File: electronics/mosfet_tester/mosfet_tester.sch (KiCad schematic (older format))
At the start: 8 parts, among them J101 BARREL_JACK, J102 CONN_01X06, J103 Screw_Terminal_1x01, J104 Screw_Terminal_1x01, U101 7805

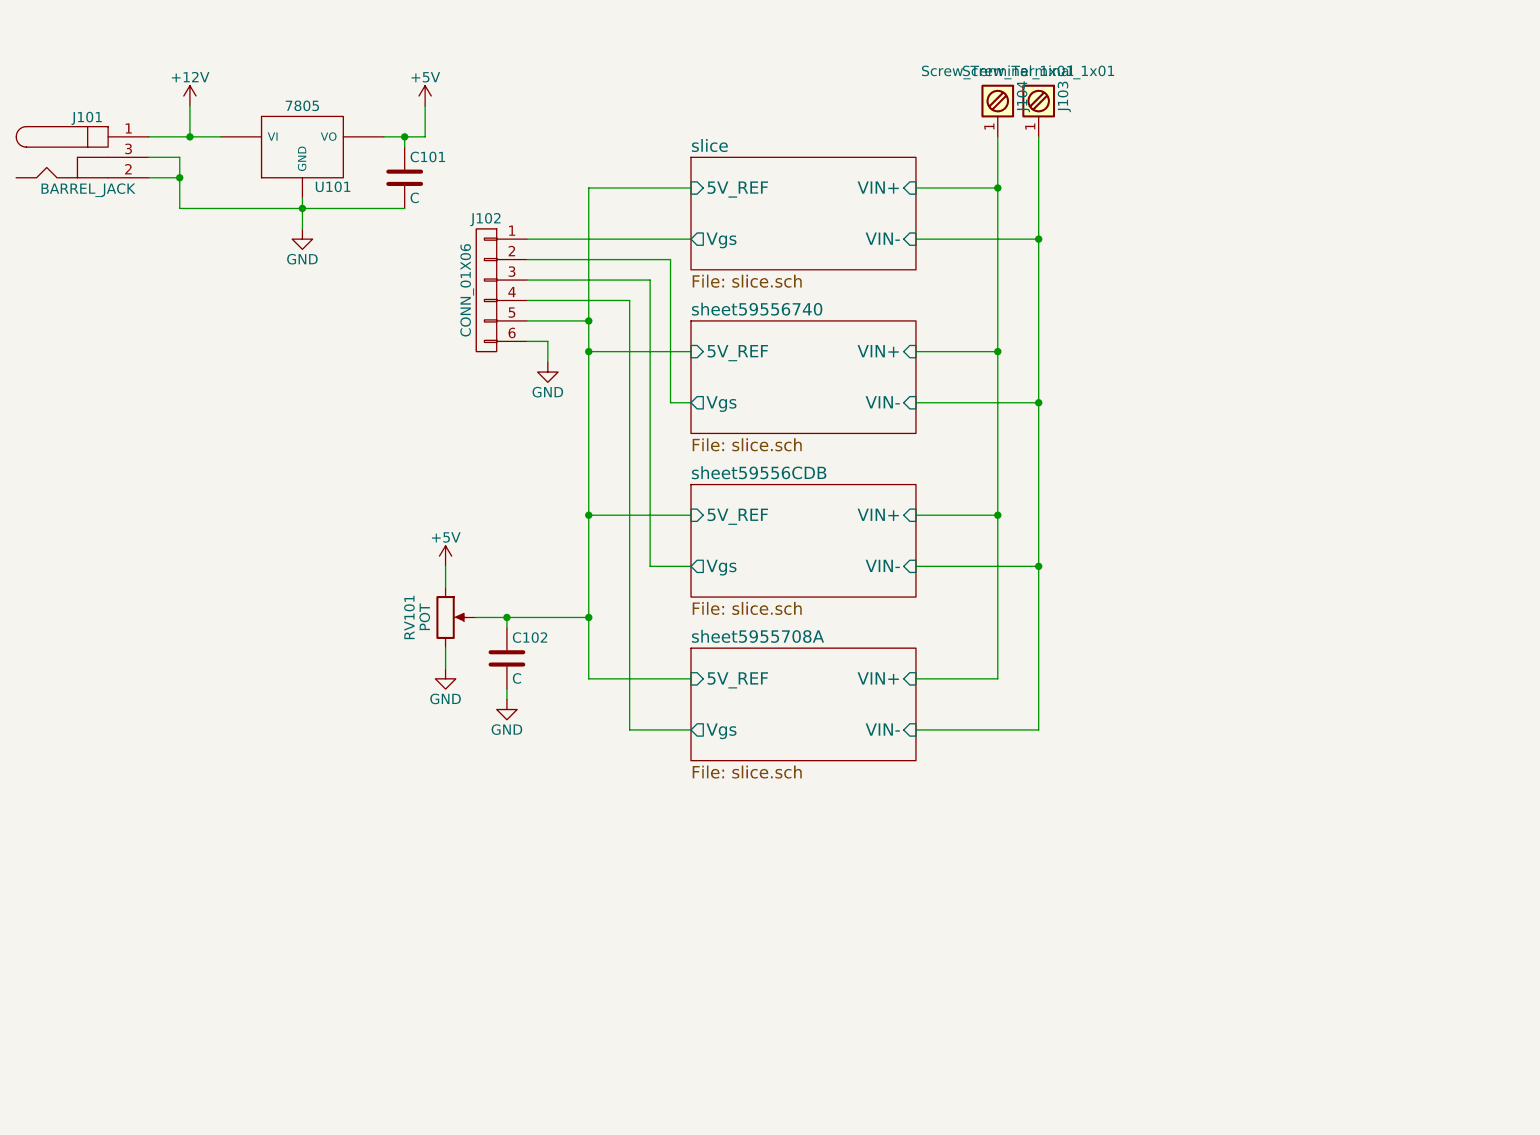
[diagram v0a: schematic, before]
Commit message: mosfet tester progress
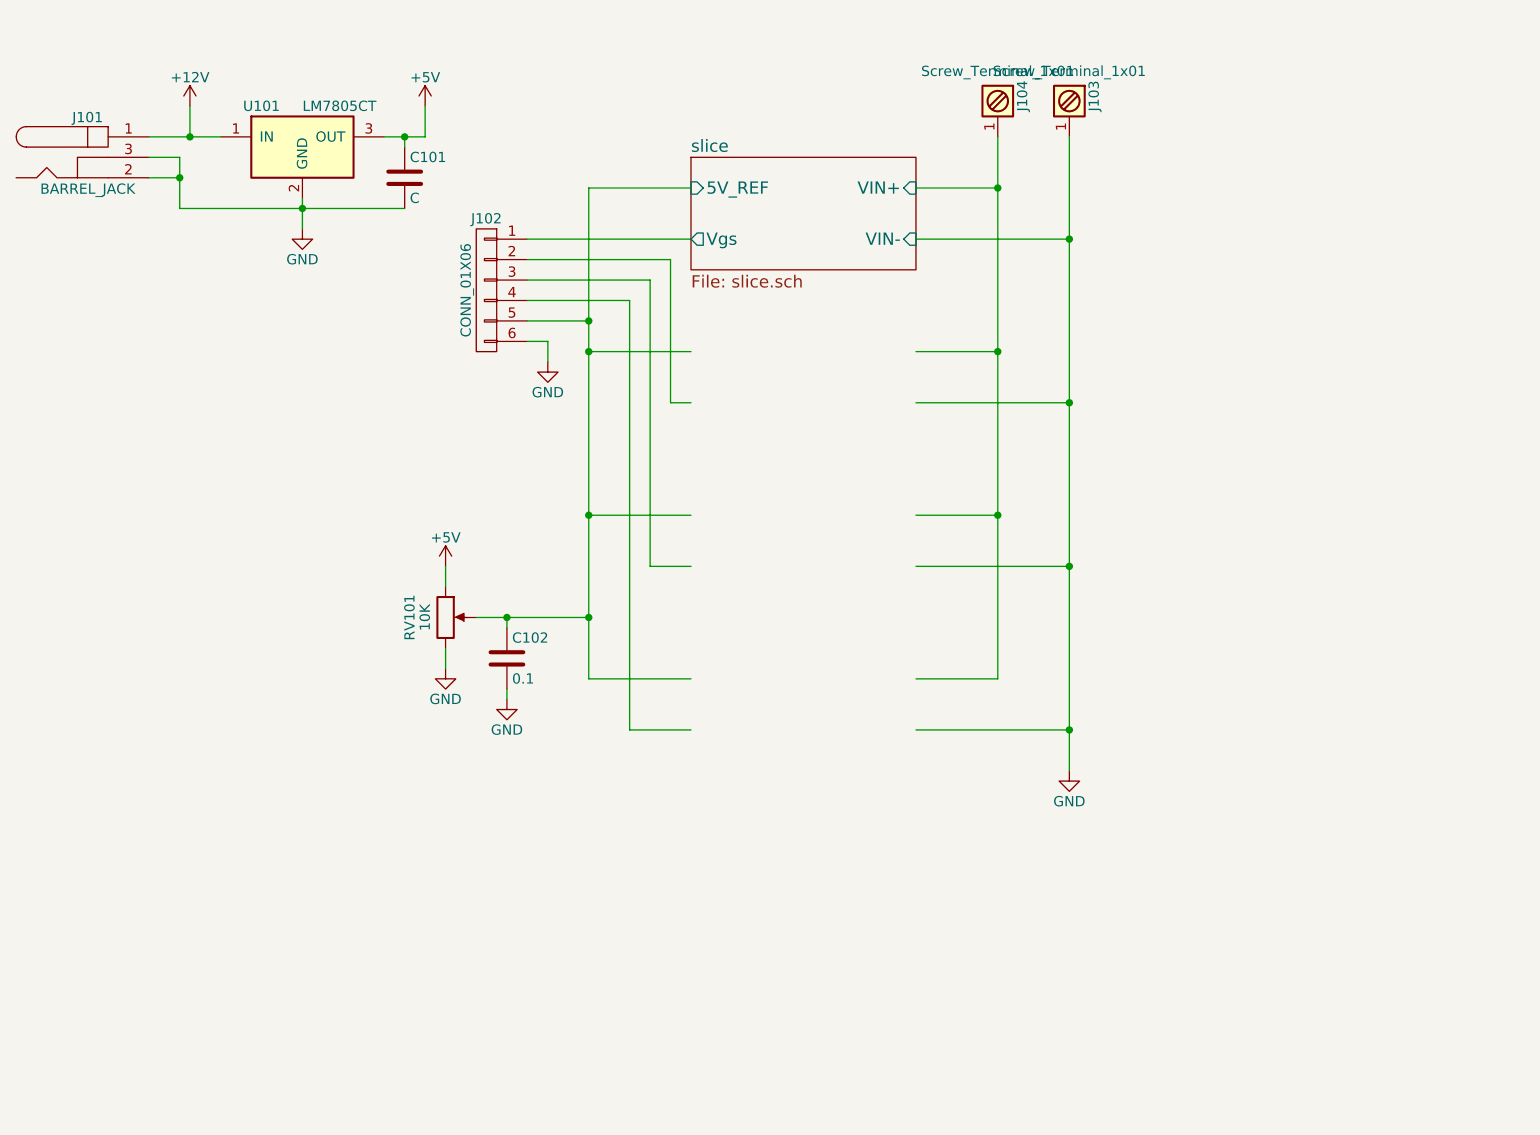
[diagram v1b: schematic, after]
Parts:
- removed U101: 7805, symbol 7805
- added U101: LM7805CT, TO_SOT_Packages_SMD:SOT-223-3Lead_TabPin2, symbol LM7805CT
- C102: value C -> 0.1
- J101: footprint (none) -> Connectors:BARREL_JACK
- RV101: value POT -> 10K; footprint (none) -> Potentiometers:Potentiometer_Trimmer_Bourns_3339P_Horizontal
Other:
- moved on the sheet: J103
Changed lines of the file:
@@
 $Descr A4 11693 8268
 encoding utf-8
-Sheet 1 5
+Sheet 1 2
 Title ""
 Date ""
@@
 F5 "Vgs" O L 5300 2550 60
 $EndSheet
-$Sheet
-S 5300 2950 1100 550
-U 59556746
-F0 "sheet59556740" 60
-F1 "slice.sch" 60
-F2 "5V_REF" I L 5300 3100 60
-F3 "VIN-" I R 6400 3350 60
-F4 "VIN+" I R 6400 3100 60
-F5 "Vgs" O L 5300 3350 60
-$EndSheet
-$Sheet
-S 5300 3750 1100 550
-U 59556CE1
-F0 "sheet59556CDB" 60
-F1 "slice.sch" 60
-F2 "5V_REF" I L 5300 3900 60
-F3 "VIN-" I R 6400 4150 60
-F4 "VIN+" I R 6400 3900 60
-F5 "Vgs" O L 5300 4150 60
-$EndSheet
-$Sheet
-S 5300 4550 1100 550
-U 59557090
-F0 "sheet5955708A" 60
-F1 "slice.sch" 60
-F2 "5V_REF" I L 5300 4700 60
-F3 "VIN-" I R 6400 4950 60
-F4 "VIN+" I R 6400 4700 60
-F5 "Vgs" O L 5300 4950 60
-$EndSheet
 $Comp
 L BARREL_JACK J101
@@
 F 0 "J101" H 2350 2345 50  0000 C CNN
 F 1 "BARREL_JACK" H 2350 1995 50  0000 C CNN
-F 2 "" H 2350 2150 50  0001 C CNN
+F 2 "Connectors:BARREL_JACK" H 2350 2150 50  0001 C CNN
 F 3 "" H 2350 2150 50  0001 C CNN
 	1    2350 2150
@@
 $EndComp
 $Comp
-L 7805 U101
-U 1 1 59558103
-P 3400 2100
-F 0 "U101" H 3550 1904 50  0000 C CNN
-F 1 "7805" H 3400 2300 50  0000 C CNN
-F 2 "" H 3400 2100 50  0001 C CNN
-F 3 "" H 3400 2100 50  0001 C CNN
-	1    3400 2100
-	1    0    0    -1
-$EndComp
-$Comp
-L +12V #PWR101
+L +12V #PWR01
 U 1 1 595581A4
 P 2850 1900
-F 0 "#PWR101" H 2850 1750 50  0001 C CNN
+F 0 "#PWR01" H 2850 1750 50  0001 C CNN
 F 1 "+12V" H 2850 2040 50  0000 C CNN
 F 2 "" H 2850 1900 50  0001 C CNN
@@
 $EndComp
 $Comp
-L +5V #PWR103
+L +5V #PWR02
 U 1 1 5955821C
 P 4000 1900
-F 0 "#PWR103" H 4000 1750 50  0001 C CNN
+F 0 "#PWR02" H 4000 1750 50  0001 C CNN
 F 1 "+5V" H 4000 2040 50  0000 C CNN
 F 2 "" H 4000 1900 50  0001 C CNN
@@
 Connection ~ 2800 2250
 $Comp
-L GND #PWR102
+L GND #PWR03
 U 1 1 5955853E
 P 3400 2500
-F 0 "#PWR102" H 3400 2250 50  0001 C CNN
+F 0 "#PWR03" H 3400 2250 50  0001 C CNN
 F 1 "GND" H 3400 2350 50  0000 C CNN
 F 2 "" H 3400 2500 50  0001 C CNN
@@
 P 4100 4400
 F 0 "RV101" V 3925 4400 50  0000 C CNN
-F 1 "POT" V 4000 4400 50  0000 C CNN
-F 2 "" H 4100 4400 50  0001 C CNN
+F 1 "10K" V 4000 4400 50  0000 C CNN
+F 2 "Potentiometers:Potentiometer_Trimmer_Bourns_3339P_Horizontal" H 4100 4400 50  0001 C CNN
 F 3 "" H 4100 4400 50  0001 C CNN
 	1    4100 4400
@@
 $EndComp
 $Comp
-L +5V #PWR104
+L +5V #PWR04
 U 1 1 59558EEF
 P 4100 4150
-F 0 "#PWR104" H 4100 4000 50  0001 C CNN
+F 0 "#PWR04" H 4100 4000 50  0001 C CNN
 F 1 "+5V" H 4100 4290 50  0000 C CNN
 F 2 "" H 4100 4150 50  0001 C CNN
@@
 	4100 4150 4100 4250
 $Comp
-L GND #PWR105
+L GND #PWR05
 U 1 1 59559020
 P 4100 4650
-F 0 "#PWR105" H 4100 4400 50  0001 C CNN
+F 0 "#PWR05" H 4100 4400 50  0001 C CNN
 F 1 "GND" H 4100 4500 50  0000 C CNN
 F 2 "" H 4100 4650 50  0001 C CNN
@@
 P 4400 4600
 F 0 "C102" H 4425 4700 50  0000 L CNN
-F 1 "C" H 4425 4500 50  0000 L CNN
+F 1 "0.1" H 4425 4500 50  0000 L CNN
 F 2 "Capacitors_SMD_Round:C_0603" H 4438 4450 50  0001 C CNN
 F 3 "" H 4400 4600 50  0001 C CNN
@@
 Connection ~ 4400 4400
 $Comp
-L GND #PWR106
+L GND #PWR06
 U 1 1 59559A94
 P 4400 4800
-F 0 "#PWR106" H 4400 4550 50  0001 C CNN
+F 0 "#PWR06" H 4400 4550 50  0001 C CNN
 F 1 "GND" H 4400 4650 50  0000 C CNN
 F 2 "" H 4400 4800 50  0001 C CNN
@@
 Connection ~ 6800 2300
 Wire Wire Line
-	7000 2050 7000 4950
-Wire Wire Line
-	7000 4950 6400 4950
-Wire Wire Line
-	6400 4150 7000 4150
-Connection ~ 7000 4150
-Wire Wire Line
-	6400 3350 7000 3350
-Connection ~ 7000 3350
-Wire Wire Line
-	6400 2550 7000 2550
-Connection ~ 7000 2550
+	7150 2050 7150 5150
+Wire Wire Line
+	7150 4950 6400 4950
+Wire Wire Line
+	6400 4150 7150 4150
+Connection ~ 7150 4150
+Wire Wire Line
+	6400 3350 7150 3350
+Connection ~ 7150 3350
+Wire Wire Line
+	6400 2550 7150 2550
+Connection ~ 7150 2550
 $Comp
 L CONN_01X06 J102
@@
 Connection ~ 4800 2950
 $Comp
-L GND #PWR107
+L GND #PWR07
 U 1 1 59555708
 P 4600 3150
-F 0 "#PWR107" H 4600 2900 50  0001 C CNN
+F 0 "#PWR07" H 4600 2900 50  0001 C CNN
 F 1 "GND" H 4600 3000 50  0000 C CNN
 F 2 "" H 4600 3150 50  0001 C CNN
@@
 L Screw_Terminal_1x01 J103
 U 1 1 59556BAD
-P 7000 1850
-F 0 "J103" H 7000 2000 50  0000 C TNN
-F 1 "Screw_Terminal_1x01" V 6850 1850 50  0000 C TNN
-F 2 "Screw_Connectors:4_Pin_Screw_Connector" H 7000 1725 50  0001 C CNN
-F 3 "" H 7000 1750 50  0001 C CNN
-	1    7000 1850
+P 7150 1850
+F 0 "J103" H 7150 2000 50  0000 C TNN
+F 1 "Screw_Terminal_1x01" V 7000 1850 50  0000 C TNN
+F 2 "Screw_Connectors:4_Pin_Screw_Connector" H 7150 1725 50  0001 C CNN
+F 3 "" H 7150 1750 50  0001 C CNN
+	1    7150 1850
 	0    1    1    0
 $EndComp
+$Comp
+L LM7805CT U101
+U 1 1 595F18FF
+P 3400 2100
+F 0 "U101" H 3200 2300 50  0000 C CNN
+F 1 "LM7805CT" H 3400 2300 50  0000 L CNN
+F 2 "TO_SOT_Packages_SMD:SOT-223-3Lead_TabPin2" H 3400 2200 50  0001 C CIN
+F 3 "" H 3400 2100 50  0001 C CNN
+	1    3400 2100
+	1    0    0    -1
+$EndComp
+$Comp
+L GND #PWR?
+U 1 1 595F26C8
+P 7150 5150
+F 0 "#PWR?" H 7150 4900 50  0001 C CNN
+F 1 "GND" H 7150 5000 50  0000 C CNN
+F 2 "" H 7150 5150 50  0001 C CNN
+F 3 "" H 7150 5150 50  0001 C CNN
+	1    7150 5150
+	1    0    0    -1
+$EndComp
+Connection ~ 7150 4950
 $EndSCHEMATC

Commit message: Rework entire board, still in progress
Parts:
- removed J102: CONN_01X06, Connectors_Molex:Molex_KK-6410-06_06x2.54mm_Straight, symbol CONN_01X06
- removed U101: LM7805CT, TO_SOT_Packages_SMD:SOT-223-3Lead_TabPin2, symbol LM7805CT
- added C102: 0.1u, Capacitors_SMD_Round:C_0603, symbol C
- added J?: CONN_01X03, Connectors_Molex:Molex_KK-6410-03_03x2.54mm_Straight, symbol CONN_01X03
- added P101: OSHW, Symbols:OSHW-Logo_7.5x8mm_SilkScreen, symbol SYMBOL
- added R101: 0R, Resistors_SMD:R_0805_HandSoldering, symbol R
- added U101: MCP1703A-3302/MB, TO_SOT_Packages_SMD:SOT89-3_Housing, symbol MCP1703A-3302/MB
- C101: value C -> 22u
- J103: renamed from J104; footprint Screw_Connectors:4_Pin_Screw_Connector -> Screw_Connectors:2_Pin_Quick_Fit
- J104: renamed from J103; footprint Screw_Connectors:4_Pin_Screw_Connector -> Screw_Connectors:2_Pin_Quick_Fit
- RV101: footprint Potentiometers:Potentiometer_Trimmer_Bourns_3339P_Horizontal -> Potentiometers:Potentiometer_Alps_RK163_Double_Vertical
- renumbered C102 to C103
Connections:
- wire segments 43 -> 65
- no-connect marks 0 -> 4
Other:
- moved on the sheet: C103, J103, J104, RV101

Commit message: Checkpoint mosfet tester
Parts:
- removed U101: MCP1703A-3302/MB, TO_SOT_Packages_SMD:SOT89-3_Housing, symbol MCP1703A-3302/MB
- added M1: BuckModule, Buck_Modules:Buck_Module_7805_Replacement_Universal, symbol BuckModule
- gave numbers to parts that had none: 1
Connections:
- wire segments 65 -> 47
- no-connect marks 4 -> 5
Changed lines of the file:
@@
 LIBS:valves
 LIBS:zeropin
+LIBS:buckmodule
 LIBS:mosfet_tester-cache
 EELAYER 25 0
@@
 $EndComp
 $Comp
-L +12V #PWR01
+L +12V #PWR1
 U 1 1 595581A4
 P 2850 1900
-F 0 "#PWR01" H 2850 1750 50  0001 C CNN
+F 0 "#PWR1" H 2850 1750 50  0001 C CNN
 F 1 "+12V" H 2850 2040 50  0000 C CNN
 F 2 "" H 2850 1900 50  0001 C CNN
@@
 $EndComp
 $Comp
-L +5V #PWR02
+L +5V #PWR3
 U 1 1 5955821C
 P 4450 1900
-F 0 "#PWR02" H 4450 1750 50  0001 C CNN
+F 0 "#PWR3" H 4450 1750 50  0001 C CNN
 F 1 "+5V" H 4450 2040 50  0000 C CNN
 F 2 "" H 4450 1900 50  0001 C CNN
@@
 $EndComp
 $Comp
-L GND #PWR03
+L GND #PWR2
 U 1 1 5955853E
 P 3400 2500
-F 0 "#PWR03" H 3400 2250 50  0001 C CNN
+F 0 "#PWR2" H 3400 2250 50  0001 C CNN
 F 1 "GND" H 3400 2350 50  0000 C CNN
 F 2 "" H 3400 2500 50  0001 C CNN
@@
 $EndComp
 $Comp
-L +5V #PWR04
+L +5V #PWR4
 U 1 1 59558EEF
 P 5850 4350
-F 0 "#PWR04" H 5850 4200 50  0001 C CNN
+F 0 "#PWR4" H 5850 4200 50  0001 C CNN
 F 1 "+5V" H 5850 4490 50  0000 C CNN
 F 2 "" H 5850 4350 50  0001 C CNN
@@
 $EndComp
 $Comp
-L GND #PWR05
+L GND #PWR5
 U 1 1 59559020
 P 5850 4850
-F 0 "#PWR05" H 5850 4600 50  0001 C CNN
+F 0 "#PWR5" H 5850 4600 50  0001 C CNN
 F 1 "GND" H 5850 4700 50  0000 C CNN
 F 2 "" H 5850 4850 50  0001 C CNN
@@
 $EndComp
 $Comp
-L GND #PWR06
+L GND #PWR6
 U 1 1 59559A94
 P 6150 5000
-F 0 "#PWR06" H 6150 4750 50  0001 C CNN
+F 0 "#PWR6" H 6150 4750 50  0001 C CNN
 F 1 "GND" H 6150 4850 50  0000 C CNN
 F 2 "" H 6150 5000 50  0001 C CNN
@@
 $EndComp
 $Comp
-L GND #PWR07
+L GND #PWR8
 U 1 1 59555708
 P 6350 3350
-F 0 "#PWR07" H 6350 3100 50  0001 C CNN
+F 0 "#PWR8" H 6350 3100 50  0001 C CNN
 F 1 "GND" H 6350 3200 50  0000 C CNN
 F 2 "" H 6350 3350 50  0001 C CNN
@@
 $EndComp
 $Comp
-L GND #PWR08
+L GND #PWR9
 U 1 1 595F26C8
 P 8900 5650
-F 0 "#PWR08" H 8900 5400 50  0001 C CNN
+F 0 "#PWR9" H 8900 5400 50  0001 C CNN
 F 1 "GND" H 8900 5500 50  0000 C CNN
 F 2 "" H 8900 5650 50  0001 C CNN
@@
 F 3 "" H 5650 6700 60  0001 C CNN
 	1    5650 6700
-	1    0    0    -1
-$EndComp
-$Comp
-L MCP1703A-3302/MB U101
-U 1 1 59811A07
-P 3400 2050
-F 0 "U101" H 3550 1800 50  0000 C CNN
-F 1 "MCP1703A-3302/MB" H 3400 2200 50  0000 C CNN
-F 2 "TO_SOT_Packages_SMD:SOT89-3_Housing" H 3450 2300 50  0001 C CNN
-F 3 "" H 3400 2000 50  0001 C CNN
-	1    3400 2050
 	1    0    0    -1
 $EndComp
@@
 $EndSheet
 $Comp
-L +12V #PWR09
+L +12V #PWR7
 U 1 1 59814FAE
 P 6300 2950
-F 0 "#PWR09" H 6300 2800 50  0001 C CNN
+F 0 "#PWR7" H 6300 2800 50  0001 C CNN
 F 1 "+12V" H 6300 3090 50  0000 C CNN
 F 2 "" H 6300 2950 50  0001 C CNN
@@
 	1    0    0    -1
 $EndComp
-Wire Wire Line
-	2650 2050 2850 2050
-Wire Wire Line
-	2850 2050 3100 2050
-Wire Wire Line
-	2850 1900 2850 2050
-Connection ~ 2850 2050
-Wire Wire Line
-	4450 2050 4450 1900
-Wire Wire Line
-	3700 2050 3900 2050
-Wire Wire Line
-	3900 2050 4250 2050
-Wire Wire Line
-	4250 2050 4450 2050
-Wire Wire Line
-	2650 2150 2800 2150
-Wire Wire Line
-	2800 2150 2800 2250
-Wire Wire Line
-	2800 2250 2800 2400
-Wire Wire Line
-	2800 2400 3400 2400
-Wire Wire Line
-	3400 2400 3900 2400
-Wire Wire Line
-	3900 2400 4250 2400
-Wire Wire Line
-	3400 2350 3400 2400
-Wire Wire Line
-	3400 2400 3400 2500
-Wire Wire Line
-	2650 2250 2800 2250
-Connection ~ 2800 2250
-Connection ~ 3400 2400
-Wire Wire Line
-	3900 2100 3900 2050
-Connection ~ 3900 2050
-Wire Wire Line
-	5850 4350 5850 4450
-Wire Wire Line
-	5850 4850 5850 4750
-Wire Wire Line
-	7050 2500 6550 2500
-Wire Wire Line
-	6550 2500 6550 3150
-Wire Wire Line
-	6550 3150 6550 3300
-Wire Wire Line
-	6550 3300 6550 4100
-Wire Wire Line
-	6550 4100 6550 4600
-Wire Wire Line
-	6550 4600 6550 4900
-Wire Wire Line
-	6550 4900 7050 4900
-Wire Wire Line
-	6000 4600 6150 4600
-Wire Wire Line
-	6150 4600 6550 4600
-Wire Wire Line
-	7050 3300 6550 3300
-Connection ~ 6550 3300
-Wire Wire Line
-	7050 4100 6550 4100
-Connection ~ 6550 4100
-Wire Wire Line
-	6150 4650 6150 4600
-Connection ~ 6150 4600
-Wire Wire Line
-	6150 5000 6150 4950
-Wire Wire Line
-	8550 2250 8550 2500
-Wire Wire Line
-	8550 2500 8550 3300
-Wire Wire Line
-	8550 3300 8550 4100
-Wire Wire Line
-	8550 4100 8550 4900
-Wire Wire Line
-	8550 4900 8150 4900
-Wire Wire Line
-	8550 4100 8150 4100
-Connection ~ 8550 4100
-Wire Wire Line
-	8150 3300 8550 3300
-Connection ~ 8550 3300
-Wire Wire Line
-	8150 2500 8550 2500
-Connection ~ 8550 2500
-Wire Wire Line
-	8900 2250 8900 2750
-Wire Wire Line
-	8900 2750 8900 3550
-Wire Wire Line
-	8900 3550 8900 4350
-Wire Wire Line
-	8900 4350 8900 5150
-Wire Wire Line
-	8900 5150 8900 5250
-Wire Wire Line
-	8900 5150 8150 5150
-Wire Wire Line
-	8150 4350 8900 4350
-Connection ~ 8900 4350
-Wire Wire Line
-	8150 3550 8900 3550
-Connection ~ 8900 3550
-Wire Wire Line
-	8150 2750 8900 2750
-Connection ~ 8900 2750
-Wire Wire Line
-	7050 3550 6950 3550
-Wire Wire Line
-	6950 3550 6950 2850
-Wire Wire Line
-	6850 4350 7050 4350
-Wire Wire Line
-	6850 4350 6850 2950
-Wire Wire Line
-	6750 3050 6750 5150
-Wire Wire Line
-	6750 5150 7050 5150
-Connection ~ 6550 3150
-Wire Wire Line
-	6350 3350 6350 3250
-Wire Wire Line
-	6350 3250 6250 3250
-Connection ~ 6550 4600
-Connection ~ 8900 5150
-Wire Wire Line
-	8900 5650 8900 5550
-Wire Wire Line
-	6300 2950 6300 3050
-Wire Wire Line
-	6300 3050 6250 3050
 $Comp
 L C C102
@@
 	1    0    0    -1
 $EndComp
-Wire Wire Line
-	4250 2100 4250 2050
-Connection ~ 4250 2050
-Connection ~ 3900 2400
-$Comp
-L CONN_01X03 J?
+$Comp
+L CONN_01X03 J1
 U 1 1 5981A06C
 P 6050 3150
-F 0 "J?" H 6050 3350 50  0000 C CNN
+F 0 "J1" H 6050 3350 50  0000 C CNN
 F 1 "CONN_01X03" V 6150 3150 50  0000 C CNN
 F 2 "Connectors_Molex:Molex_KK-6410-03_03x2.54mm_Straight" H 6050 3150 50  0001 C CNN
@@
 	-1   0    0    -1
 $EndComp
-Wire Wire Line
-	6550 3150 6250 3150
-Wire Wire Line
-	7050 2750 6750 2750
-Wire Wire Line
-	6850 2950 6750 2950
-Wire Wire Line
-	6950 2850 6750 2850
 NoConn ~ 6750 2750
 NoConn ~ 6750 2850
 NoConn ~ 6750 2950
 NoConn ~ 6750 3050
+Wire Wire Line
+	2850 2050 2850 1900
+Wire Wire Line
+	4450 2050 4450 1900
+Wire Wire Line
+	3850 2050 4450 2050
+Wire Wire Line
+	2650 2150 2800 2150
+Wire Wire Line
+	2800 2150 2800 2400
+Wire Wire Line
+	2800 2400 4250 2400
+Wire Wire Line
+	3400 2400 3400 2500
+Wire Wire Line
+	2650 2250 2800 2250
+Connection ~ 2800 2250
+Connection ~ 3400 2400
+Wire Wire Line
+	3900 2100 3900 2050
+Connection ~ 3900 2050
+Wire Wire Line
+	5850 4350 5850 4450
+Wire Wire Line
+	5850 4850 5850 4750
+Wire Wire Line
+	7050 2500 6550 2500
+Wire Wire Line
+	6550 2500 6550 4900
+Wire Wire Line
+	6550 4900 7050 4900
+Wire Wire Line
+	6000 4600 6550 4600
+Wire Wire Line
+	7050 3300 6550 3300
+Connection ~ 6550 3300
+Wire Wire Line
+	7050 4100 6550 4100
+Connection ~ 6550 4100
+Wire Wire Line
+	6150 4650 6150 4600
+Connection ~ 6150 4600
+Wire Wire Line
+	6150 5000 6150 4950
+Wire Wire Line
+	8550 2250 8550 4900
+Wire Wire Line
+	8550 4900 8150 4900
+Wire Wire Line
+	8550 4100 8150 4100
+Connection ~ 8550 4100
+Wire Wire Line
+	8150 3300 8550 3300
+Connection ~ 8550 3300
+Wire Wire Line
+	8150 2500 8550 2500
+Connection ~ 8550 2500
+Wire Wire Line
+	8900 2250 8900 5250
+Wire Wire Line
+	8900 5150 8150 5150
+Wire Wire Line
+	8150 4350 8900 4350
+Connection ~ 8900 4350
+Wire Wire Line
+	8150 3550 8900 3550
+Connection ~ 8900 3550
+Wire Wire Line
+	8150 2750 8900 2750
+Connection ~ 8900 2750
+Wire Wire Line
+	7050 3550 6950 3550
+Wire Wire Line
+	6950 3550 6950 2850
+Wire Wire Line
+	6850 4350 7050 4350
+Wire Wire Line
+	6850 4350 6850 2950
+Wire Wire Line
+	6750 3050 6750 5150
+Wire Wire Line
+	6750 5150 7050 5150
+Connection ~ 6550 3150
+Wire Wire Line
+	6350 3350 6350 3250
+Wire Wire Line
+	6350 3250 6250 3250
+Connection ~ 6550 4600
+Connection ~ 8900 5150
+Wire Wire Line
+	8900 5650 8900 5550
+Wire Wire Line
+	6300 2950 6300 3050
+Wire Wire Line
+	6300 3050 6250 3050
+Wire Wire Line
+	4250 2100 4250 2050
+Connection ~ 4250 2050
+Connection ~ 3900 2400
+Wire Wire Line
+	6550 3150 6250 3150
+Wire Wire Line
+	7050 2750 6750 2750
+Wire Wire Line
+	6850 2950 6750 2950
+Wire Wire Line
+	6950 2850 6750 2850
+$Comp
+L BuckModule M1
+U 1 1 59961E07
+P 3400 2050
+F 0 "M1" H 3400 2250 60  0000 C CNN
+F 1 "BuckModule" H 3400 1850 60  0000 C CNN
+F 2 "Buck_Modules:Buck_Module_7805_Replacement_Universal" H 3400 2100 60  0001 C CNN
+F 3 "" H 3400 2100 60  0001 C CNN
+	1    3400 2050
+	1    0    0    -1
+$EndComp
+Wire Wire Line
+	2950 2000 2850 2000
+Connection ~ 2850 2000
+Wire Wire Line
+	2650 2050 2850 2050
+NoConn ~ 2950 2100
 $EndSCHEMATC
